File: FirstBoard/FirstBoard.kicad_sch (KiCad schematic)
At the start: 26 parts, among them J0 Battery, J1 MPU0, J10 MPU9, J11 MPU10, J12 MPU11, J13 MPU12, J15 SD_CARD, J2 MPU1, J3 MPU3, J4 MPU3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

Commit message: Finished V2
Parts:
- removed SW1: SW_MEC_5E, symbol Switch:SW_MEC_5E
- removed SW2: ON/OFF Switch, symbol Switch:SW_MEC_5G
- added SW1: SW_Push, Button_Switch_THT:SW_PUSH_6mm_H5mm, symbol Switch:SW_Push
- added SW2: ON/OFF, TCC_FOOTPRINTS:BOTAO-ONOFF, symbol Switch:SW_Push
- R1: footprint (none) -> Resistor_THT:R_Axial_DIN0207_L6.3mm_D2.5mm_P10.16mm_Horizontal
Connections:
- net 3v3: now also SW1.1
- net BAT+: now also SW2.1
- net Switch: now also SW1.2
- net at U2.1 (IN+): now also SW2.2
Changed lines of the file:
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@@
   (junction (at 13.97 31.75) (diameter 0) (color 0 0 0 0)
-  )
-  (junction (at 106.68 96.52) (diameter 0) (color 0 0 0 0)
-  )
-  (junction (at 96.52 93.98) (diameter 0) (color 0 0 0 0)
   )
   (wire (pts (xy 44.45 83.82) (xy 44.45 85.09))
@@
   )
   (wire (pts (xy 92.71 93.98) (xy 96.52 93.98))
-    (stroke (width 0) (type default) (color 0 0 0 0))
-  )
-  (wire (pts (xy 96.52 93.98) (xy 96.52 96.52))
     (stroke (width 0) (type default) (color 0 0 0 0))
   )
@@
     (pin "1")
   )
-  (symbol (lib_id "Switch:SW_MEC_5G") (at 116.84 31.75 0) (unit 1)
-    (in_bom yes) (on_board yes) (fields_autoplaced)
-    (property "Reference" "SW2" (id 0) (at 116.84 24.13 0))
-    (property "Value" "ON/OFF Switch" (id 1) (at 116.84 26.67 0))
-    (property "Footprint" "" (id 2) (at 116.84 26.67 0)
-      (effects (font (size 1.27 1.27)) hide)
-    )
-    (property "Datasheet" "http://www.apem.com/int/index.php?controller=attachment&id_attachment=488" (id 3) (at 116.84 26.67 0)
-      (effects (font (size 1.27 1.27)) hide)
-    )
-    (pin "1")
-    (pin "3")
-    (pin "2")
-    (pin "4")
-  )
   (symbol (lib_id "power:GND") (at 72.39 186.69 0) (unit 1)
     (in_bom yes) (on_board yes) (fields_autoplaced)
@@
     )
     (pin "1")
+  )
+  (symbol (lib_id "Switch:SW_Push") (at 101.6 93.98 0) (unit 1)
+    (in_bom yes) (on_board yes) (fields_autoplaced)
+    (property "Reference" "SW1" (id 0) (at 101.6 86.36 0))
+    (property "Value" "SW_Push" (id 1) (at 101.6 88.9 0))
+    (property "Footprint" "Button_Switch_THT:SW_PUSH_6mm_H5mm" (id 2) (at 101.6 88.9 0)
+      (effects (font (size 1.27 1.27)) hide)
+    )
+    (property "Datasheet" "~" (id 3) (at 101.6 88.9 0)
+      (effects (font (size 1.27 1.27)) hide)
+    )
+    (pin "1")
+    (pin "2")
   )
   (symbol (lib_id "Device:R") (at 191.77 85.09 90) (unit 1)
@@
     )
     (pin "1")
-  )
-  (symbol (lib_id "Switch:SW_MEC_5E") (at 101.6 96.52 0) (unit 1)
-    (in_bom yes) (on_board yes) (fields_autoplaced)
-    (property "Reference" "SW1" (id 0) (at 101.6 86.36 0))
-    (property "Value" "SW_MEC_5E" (id 1) (at 101.6 88.9 0))
-    (property "Footprint" "" (id 2) (at 101.6 88.9 0)
-      (effects (font (size 1.27 1.27)) hide)
-    )
-    (property "Datasheet" "http://www.apem.com/int/index.php?controller=attachment&id_attachment=1371" (id 3) (at 101.6 88.9 0)
-      (effects (font (size 1.27 1.27)) hide)
-    )
-    (pin "1")
-    (pin "2")
-    (pin "3")
-    (pin "4")
   )
   (symbol (lib_id "Connector_Generic:Conn_01x06") (at 175.26 48.26 180) (unit 1)
@@
     (pin "8")
   )
+  (symbol (lib_id "Switch:SW_Push") (at 116.84 31.75 0) (unit 1)
+    (in_bom yes) (on_board yes) (fields_autoplaced)
+    (property "Reference" "SW2" (id 0) (at 116.84 24.13 0))
+    (property "Value" "ON/OFF" (id 1) (at 116.84 26.67 0))
+    (property "Footprint" "TCC_FOOTPRINTS:BOTAO-ONOFF" (id 2) (at 116.84 26.67 0)
+      (effects (font (size 1.27 1.27)) hide)
+    )
+    (property "Datasheet" "~" (id 3) (at 116.84 26.67 0)
+      (effects (font (size 1.27 1.27)) hide)
+    )
+    (pin "1")
+    (pin "2")
+  )
   (symbol (lib_id "power:GND") (at 46.99 184.15 0) (unit 1)
     (in_bom yes) (on_board yes) (fields_autoplaced)
@@
       (effects (font (size 1.27 1.27)) (justify left))
     )
-    (property "Footprint" "" (id 2) (at 104.902 100.33 90)
+    (property "Footprint" "Resistor_THT:R_Axial_DIN0207_L6.3mm_D2.5mm_P10.16mm_Horizontal" (id 2) (at 104.902 100.33 90)
       (effects (font (size 1.27 1.27)) hide)
     )
@@
     )
     (path "/b2a83418-a39c-4ba6-85d1-03d971c9ce85"
-      (reference "R1") (unit 1) (value "10k") (footprint "")
+      (reference "R1") (unit 1) (value "10k") (footprint "Resistor_THT:R_Axial_DIN0207_L6.3mm_D2.5mm_P10.16mm_Horizontal")
     )
     (path "/80a8992c-1ab2-410e-8cb7-6dfb5627a1c0"
@@
       (reference "R5") (unit 1) (value "1K8") (footprint "Resistor_THT:R_Axial_DIN0207_L6.3mm_D2.5mm_P10.16mm_Horizontal")
     )
-    (path "/4445977e-e3b5-4c71-a3e8-0f9eeafd973e"
-      (reference "SW1") (unit 1) (value "SW_MEC_5E") (footprint "")
-    )
-    (path "/2b10264d-c1fb-4be1-a930-16fdf4a061b5"
-      (reference "SW2") (unit 1) (value "ON/OFF Switch") (footprint "")
+    (path "/34db5c7f-f580-4311-ba6d-475da0633dcb"
+      (reference "SW1") (unit 1) (value "SW_Push") (footprint "Button_Switch_THT:SW_PUSH_6mm_H5mm")
+    )
+    (path "/9de1d53b-becd-42e5-afab-ff9467d21fd7"
+      (reference "SW2") (unit 1) (value "ON/OFF") (footprint "TCC_FOOTPRINTS:BOTAO-ONOFF")
     )
     (path "/01be5327-03e7-44a5-b424-ed448c86ba42"

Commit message: Few pins adjusted
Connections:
- net 3v3: now also R4.1, R5.2
- net GND: no longer R4.1, R5.2
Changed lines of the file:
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@@
+    )
+  )
+  (global_label "3v3" (shape input) (at 196.85 76.2 0) (fields_autoplaced)
+    (effects (font (size 1.27 1.27)) (justify left))
+    (property "Intersheet References" "${INTERSHEET_REFS}" (id 0) (at 202.6498 76.1206 0)
+      (effects (font (size 1.27 1.27)) (justify left) hide)
     )
   )
@@
     (property "Intersheet References" "${INTERSHEET_REFS}" (id 0) (at 134.384 102.7906 0)
       (effects (font (size 1.27 1.27)) (justify right) hide)
+    )
+  )
+  (global_label "3v3" (shape input) (at 196.85 85.09 0) (fields_autoplaced)
+    (effects (font (size 1.27 1.27)) (justify left))
+    (property "Intersheet References" "${INTERSHEET_REFS}" (id 0) (at 202.6498 85.0106 0)
+      (effects (font (size 1.27 1.27)) (justify left) hide)
     )
   )
@@
     (pin "1")
   )
-  (symbol (lib_id "power:GND") (at 196.85 85.09 0) (unit 1)
-    (in_bom yes) (on_board yes) (fields_autoplaced)
-    (property "Reference" "#PWR02" (id 0) (at 196.85 91.44 0)
-      (effects (font (size 1.27 1.27)) hide)
-    )
-    (property "Value" "GND" (id 1) (at 196.85 90.17 0)
-      (effects (font (size 1.27 1.27)) hide)
-    )
-    (property "Footprint" "" (id 2) (at 196.85 85.09 0)
-      (effects (font (size 1.27 1.27)) hide)
-    )
-    (property "Datasheet" "" (id 3) (at 196.85 85.09 0)
-      (effects (font (size 1.27 1.27)) hide)
-    )
-    (pin "1")
-  )
   (symbol (lib_id "Device:R") (at 27.94 21.59 90) (unit 1)
     (in_bom yes) (on_board yes) (fields_autoplaced)
@@
     (pin "1")
   )
-  (symbol (lib_id "power:GND") (at 196.85 76.2 0) (unit 1)
-    (in_bom yes) (on_board yes) (fields_autoplaced)
-    (property "Reference" "#PWR03" (id 0) (at 196.85 82.55 0)
-      (effects (font (size 1.27 1.27)) hide)
-    )
-    (property "Value" "GND" (id 1) (at 196.85 81.28 0)
-      (effects (font (size 1.27 1.27)) hide)
-    )
-    (property "Footprint" "" (id 2) (at 196.85 76.2 0)
-      (effects (font (size 1.27 1.27)) hide)
-    )
-    (property "Datasheet" "" (id 3) (at 196.85 76.2 0)
-      (effects (font (size 1.27 1.27)) hide)
-    )
-    (pin "1")
-  )
   (symbol (lib_id "power:GND") (at 21.59 184.15 0) (unit 1)
     (in_bom yes) (on_board yes) (fields_autoplaced)
@@
       (reference "#PWR01") (unit 1) (value "GND") (footprint "")
     )
-    (path "/801627b1-b529-4878-ac8f-950b259f172b"
-      (reference "#PWR02") (unit 1) (value "GND") (footprint "")
-    )
-    (path "/f0b09a74-1abd-4997-b696-216ef162ab41"
-      (reference "#PWR03") (unit 1) (value "GND") (footprint "")
-    )
     (path "/c3fec26b-eaf9-4b3e-bce4-9888bdcc3630"

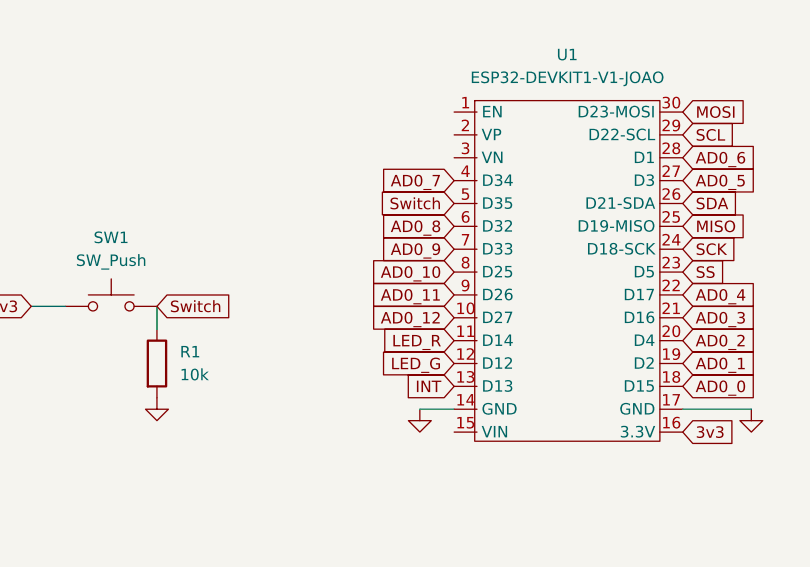
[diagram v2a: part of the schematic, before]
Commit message: Input-only pin changed
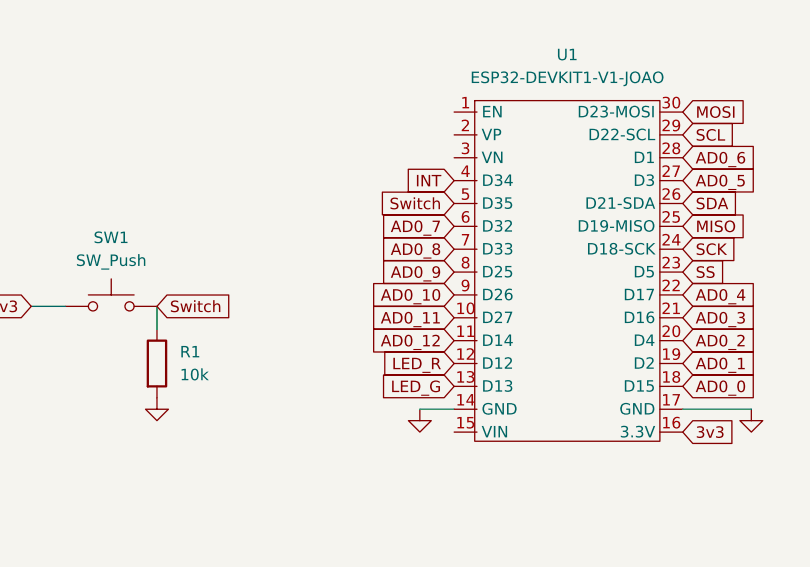
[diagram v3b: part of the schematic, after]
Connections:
- net AD0_10: now also U1.9 (D26); no longer U1.8 (D25)
- net AD0_11: now also U1.10 (D27); no longer U1.9 (D26)
- net AD0_12: now also U1.11 (D14); no longer U1.10 (D27)
- net AD0_7: now also U1.6 (D32); no longer U1.4 (D34)
- net AD0_8: now also U1.7 (D33); no longer U1.6 (D32)
- net AD0_9: now also U1.8 (D25); no longer U1.7 (D33)
- net INT: now also U1.4 (D34); no longer U1.13 (D13)
- net LED_G: now also U1.13 (D13); no longer U1.12 (D12)
- net LED_R: now also U1.12 (D12); no longer U1.11 (D14)
